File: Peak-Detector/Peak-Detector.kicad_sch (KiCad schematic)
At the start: 10 parts, among them U1 LMH6658

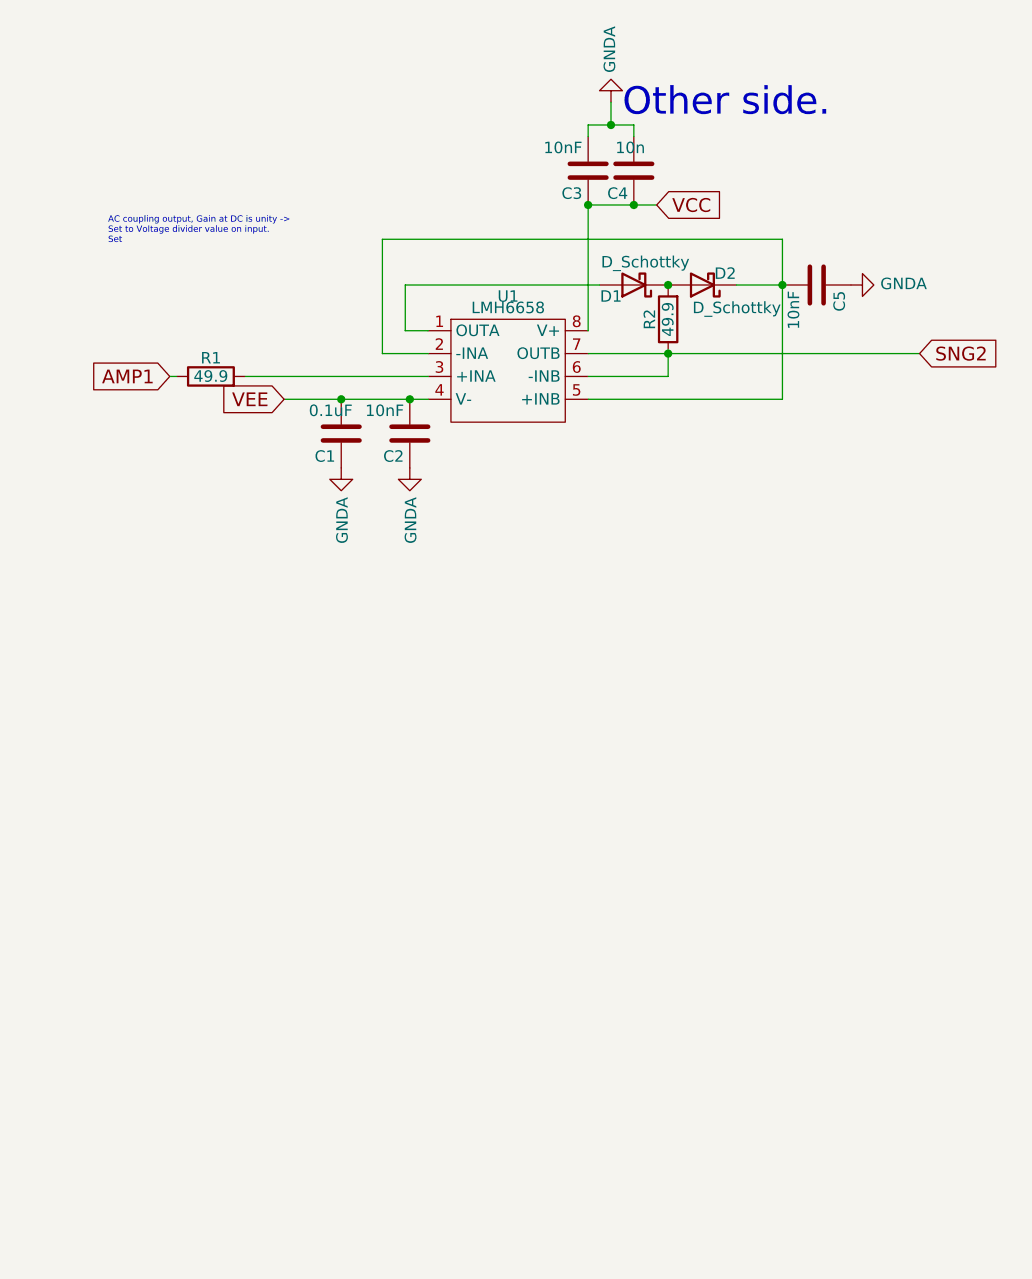
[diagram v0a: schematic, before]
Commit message: adding new peak detector schematic
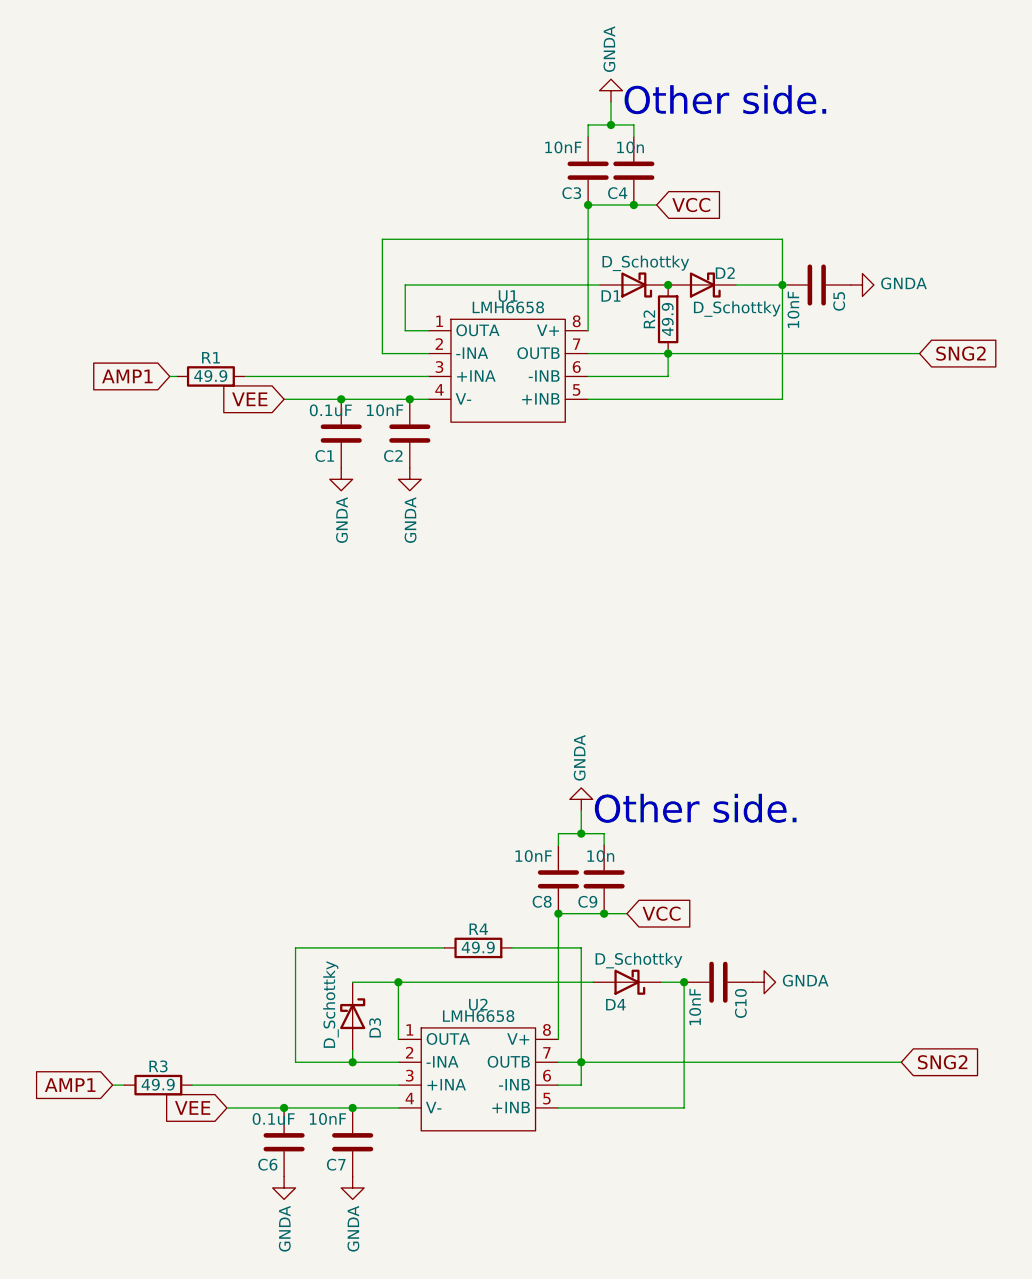
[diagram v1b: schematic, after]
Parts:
- added C10, C7, C8: 10nF, Capacitor_SMD:C_0603_1608Metric, symbol device:C
- added C6: 0.1uF, Capacitor_SMD:C_0603_1608Metric, symbol device:C
- added C9: 10n, Capacitor_SMD:C_0603_1608Metric, symbol device:C
- added D3, D4: D_Schottky, Diode_SMD:D_SOD-523, symbol My_Symbol_Library:D_Schottky
- added R3, R4: 49.9, Capacitor_SMD:C_0603_1608Metric, symbol device:R
- added U2: LMH6658, Package_SO:SOIC-8_3.9x4.9mm_P1.27mm, symbol My_Library:LMH6658
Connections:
- net AMP1: now also R3.1
- net GNDA: now also C10.1, C6.1, C7.1, C8.2, C9.2
- net SNG2: now also R4.2, U2.6 (-INB), U2.7 (OUTB)
- net VCC: now also C8.1, C9.1, U2.8 (V+)
- net VEE: now also C6.2, C7.2, U2.4 (V-)
- new net: C10.2, D4.1 (K), U2.5 (+INB)
- new net: D3.1 (K), D4.2 (A), U2.1 (OUTA)
- new net: D3.2 (A), R4.1, U2.2 (-INA)
- new net: R3.2, U2.3 (+INA)
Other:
- note removed: "AC coupling output, Gain at DC is unity -> Set to Voltage divider value on input. Set"
